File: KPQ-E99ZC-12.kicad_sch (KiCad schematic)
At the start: 25 parts, among them J1 USB Cable, J2 Chassis, J3 SWD, J4 Edge Connector, J5 Alternate Connector 1, J6 Alternate Connector 2, SW1 BOOT, U1 USBLC6-2SC6, U2 XC6206P332MR-G, U3 STM32C071KBT6

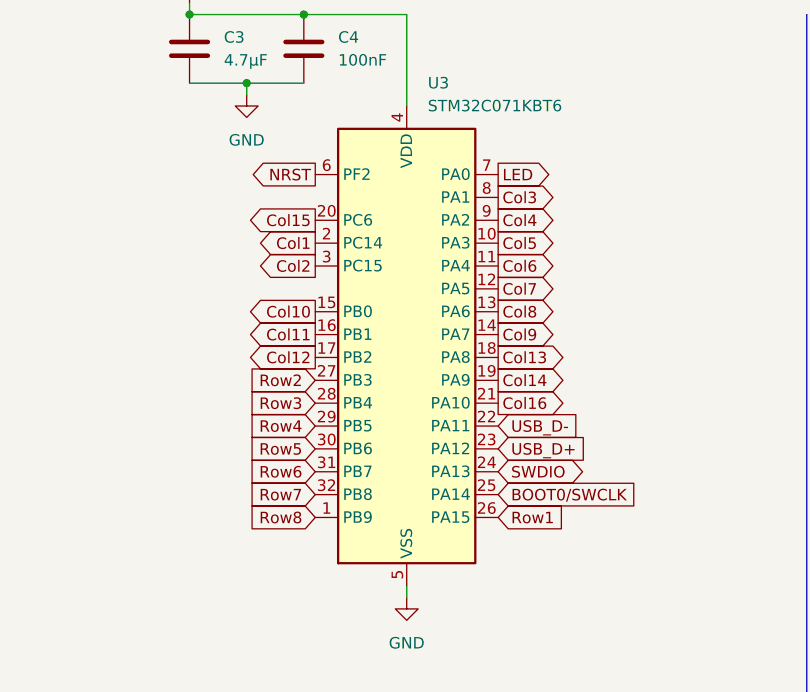
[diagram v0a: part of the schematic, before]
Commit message: Swap LED pin
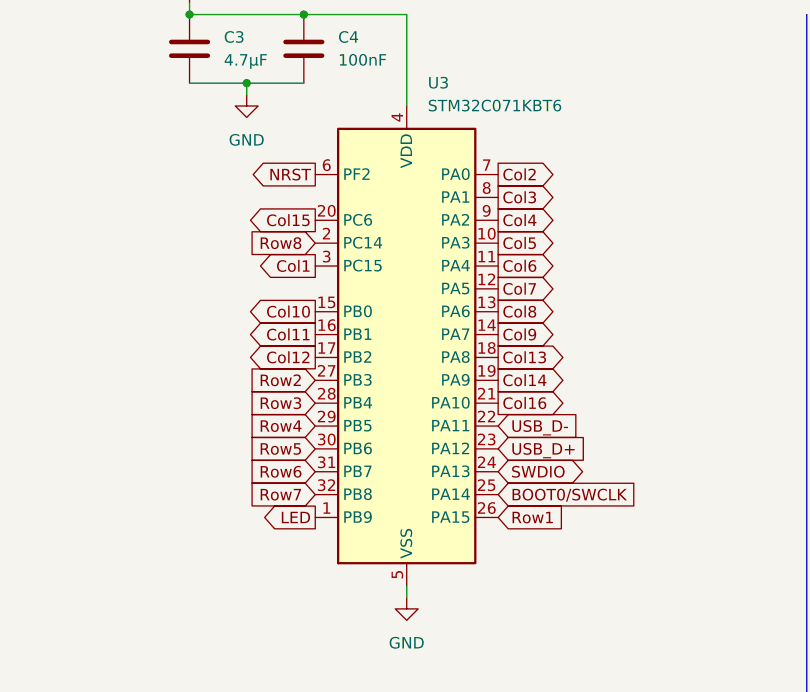
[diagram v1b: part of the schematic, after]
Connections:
- net Col1: now also U3.3 (PC15); no longer U3.2 (PC14)
- net Col2: now also U3.7 (PA0); no longer U3.3 (PC15)
- net LED: now also U3.1 (PB9); no longer U3.7 (PA0)
- net Row8: now also U3.2 (PC14); no longer U3.1 (PB9)
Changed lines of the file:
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@@
 	(global_label "Col2"
 		(shape output)
-		(at 171.45 83.82 180)
-		(fields_autoplaced yes)
-		(effects
-			(font
-				(size 1.27 1.27)
-			)
-			(justify right)
-		)
-		(property "Intersheetrefs" "${INTERSHEET_REFS}"
-			(at 165.2342 83.82 0)
-			(effects
-				(font
-					(size 1.27 1.27)
-				)
-				(justify right)
+		(at 191.77 73.66 0)
+		(fields_autoplaced yes)
+		(effects
+			(font
+				(size 1.27 1.27)
+			)
+			(justify left)
+		)
+		(property "Intersheetrefs" "${INTERSHEET_REFS}"
+			(at 197.9858 73.66 0)
+			(effects
+				(font
+					(size 1.27 1.27)
+				)
+				(justify left)
 				(hide yes)
 			)
@@
 	(global_label "Row8"
 		(shape input)
-		(at 171.45 111.76 180)
-		(fields_autoplaced yes)
-		(effects
-			(font
-				(size 1.27 1.27)
-			)
-			(justify right)
-		)
-		(property "Intersheetrefs" "${INTERSHEET_REFS}"
-			(at 164.2875 111.76 0)
+		(at 171.45 81.28 180)
+		(fields_autoplaced yes)
+		(effects
+			(font
+				(size 1.27 1.27)
+			)
+			(justify right)
+		)
+		(property "Intersheetrefs" "${INTERSHEET_REFS}"
+			(at 164.2875 81.28 0)
 			(effects
 				(font
@@
 	(global_label "LED"
 		(shape output)
-		(at 191.77 73.66 0)
-		(fields_autoplaced yes)
-		(effects
-			(font
-				(size 1.27 1.27)
-			)
-			(justify left)
-		)
-		(property "Intersheetrefs" "${INTERSHEET_REFS}"
-			(at 197.5254 73.66 0)
-			(effects
-				(font
-					(size 1.27 1.27)
-				)
-				(justify left)
+		(at 171.45 111.76 180)
+		(fields_autoplaced yes)
+		(effects
+			(font
+				(size 1.27 1.27)
+			)
+			(justify right)
+		)
+		(property "Intersheetrefs" "${INTERSHEET_REFS}"
+			(at 165.6946 111.76 0)
+			(effects
+				(font
+					(size 1.27 1.27)
+				)
+				(justify right)
 				(hide yes)
 			)
@@
 	(global_label "Col1"
 		(shape output)
-		(at 171.45 81.28 180)
-		(fields_autoplaced yes)
-		(effects
-			(font
-				(size 1.27 1.27)
-			)
-			(justify right)
-		)
-		(property "Intersheetrefs" "${INTERSHEET_REFS}"
-			(at 165.336 81.28 0)
-			(effects
-				(font
+		(at 171.45 83.82 180)
+		(fields_autoplaced yes)
+		(effects
+			(font
+				(size 1.27 1.27)
+			)
+			(justify right)
+		)
+		(property "Intersheetrefs" "${INTERSHEET_REFS}"
+			(at 165.336 83.82 0)
+			(effects
+				(font

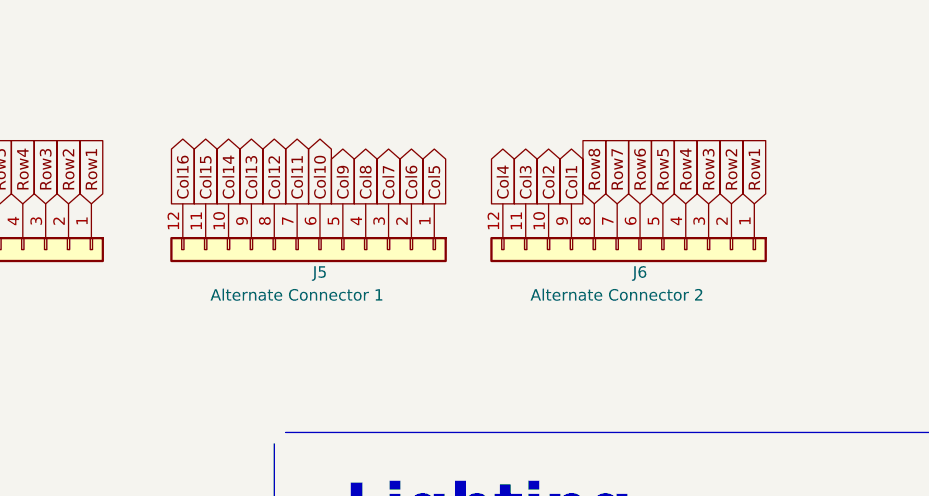
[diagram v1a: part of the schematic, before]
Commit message: Refine edges and positioning, especially around edge connectors
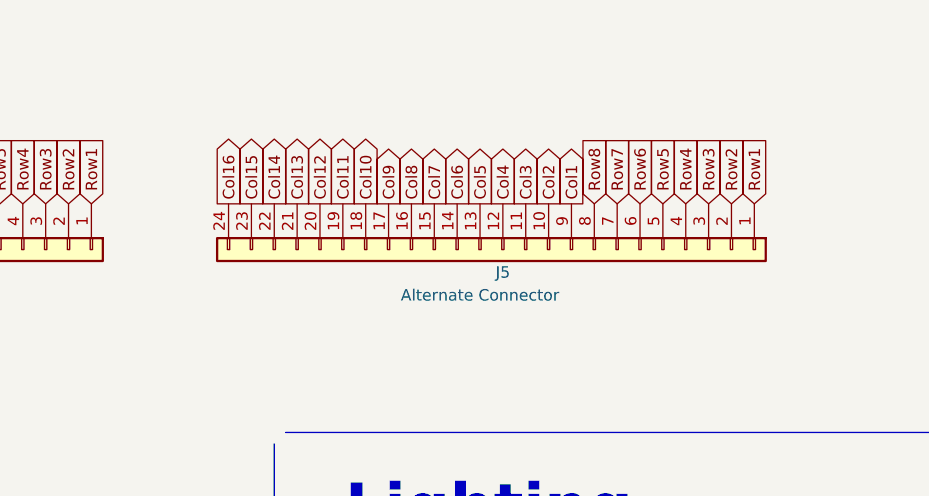
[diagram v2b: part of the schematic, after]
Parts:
- removed J5: Alternate Connector 1, Connector_PinHeader_2.54mm:PinHeader_1x12_P2.54mm_Vertical, symbol Connector_Generic:Conn_01x12
- J5: renamed from J6; value Alternate Connector 2 -> Alternate Connector; footprint Connector_PinHeader_2.54mm:PinHeader_1x12_P2.54mm_Vertical -> Connector_PinHeader_2.54mm:PinHeader_1x24_P2.54mm_Vertical; symbol Connector_Generic:Conn_01x12 -> Connector_Generic:Conn_01x24
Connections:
- net Col10: now also J5.18 (Pin_18)
- net Col11: now also J5.19 (Pin_19)
- net Col12: now also J5.20 (Pin_20)
- net Col13: now also J5.21 (Pin_21)
- net Col14: now also J5.22 (Pin_22)
- net Col15: now also J5.23 (Pin_23)
- net Col16: now also J5.24 (Pin_24)
- net Col5: now also J5.13 (Pin_13)
- net Col6: now also J5.14 (Pin_14)
- net Col7: now also J5.15 (Pin_15)
- net Col8: now also J5.16 (Pin_16)
- net Col9: now also J5.17 (Pin_17)
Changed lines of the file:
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@@
 	(global_label "Col16"
 		(shape output)
-		(at 215.9 29.21 90)
+		(at 220.98 29.21 90)
 		(fields_autoplaced yes)
 		(effects
@@
 		)
 		(property "Intersheetrefs" "${INTERSHEET_REFS}"
-			(at 215.9 22.1183 90)
+			(at 220.98 22.1183 90)
 			(effects
 				(font
@@
 	(global_label "Col8"
 		(shape output)
-		(at 236.22 29.21 90)
+		(at 241.3 29.21 90)
 		(fields_autoplaced yes)
 		(effects
@@
 		)
 		(property "Intersheetrefs" "${INTERSHEET_REFS}"
-			(at 236.22 22.8875 90)
+			(at 241.3 22.8875 90)
 			(effects
 				(font
@@
 	(global_label "Col11"
 		(shape output)
-		(at 228.6 29.21 90)
+		(at 233.68 29.21 90)
 		(fields_autoplaced yes)
 		(effects
@@
 		)
 		(property "Intersheetrefs" "${INTERSHEET_REFS}"
-			(at 228.6 22.2969 90)
+			(at 233.68 22.2969 90)
 			(effects
 				(font
@@
 	(global_label "Col13"
 		(shape output)
-		(at 223.52 29.21 90)
+		(at 228.6 29.21 90)
 		(fields_autoplaced yes)
 		(effects
@@
 		)
 		(property "Intersheetrefs" "${INTERSHEET_REFS}"
-			(at 223.52 22.1902 90)
+			(at 228.6 22.1902 90)
 			(effects
 				(font
@@
 	(global_label "Col5"
 		(shape output)
-		(at 243.84 29.21 90)
+		(at 248.92 29.21 90)
 		(fields_autoplaced yes)
 		(effects
@@
 		)
 		(property "Intersheetrefs" "${INTERSHEET_REFS}"
-			(at 243.84 22.9707 90)
+			(at 248.92 22.9707 90)
 			(effects
 				(font
@@
 	(global_label "Col7"
 		(shape output)
-		(at 238.76 29.21 90)
+		(at 243.84 29.21 90)
 		(fields_autoplaced yes)
 		(effects
@@
 		)
 		(property "Intersheetrefs" "${INTERSHEET_REFS}"
-			(at 238.76 23.0836 90)
+			(at 243.84 23.0836 90)
 			(effects
 				(font
@@
 	(global_label "Col10"
 		(shape output)
-		(at 231.14 29.21 90)
+		(at 236.22 29.21 90)
 		(fields_autoplaced yes)
 		(effects
@@
 		)
 		(property "Intersheetrefs" "${INTERSHEET_REFS}"
-			(at 231.14 22.0773 90)
+			(at 236.22 22.0773 90)
 			(effects
 				(font
@@
 	(global_label "Col15"
 		(shape output)
-		(at 218.44 29.21 90)
+		(at 223.52 29.21 90)
 		(fields_autoplaced yes)
 		(effects
@@
 		)
 		(property "Intersheetrefs" "${INTERSHEET_REFS}"
-			(at 218.44 22.1716 90)
+			(at 223.52 22.1716 90)
 			(effects
 				(font
@@
 	(global_label "Col6"
 		(shape output)
-		(at 241.3 29.21 90)
+		(at 246.38 29.21 90)
 		(fields_autoplaced yes)
 		(effects
@@
 		)
 		(property "Intersheetrefs" "${INTERSHEET_REFS}"
-			(at 241.3 22.9173 90)
+			(at 246.38 22.9173 90)
 			(effects
 				(font
@@
 	(global_label "Col9"
 		(shape output)
-		(at 233.68 29.21 90)
+		(at 238.76 29.21 90)
 		(fields_autoplaced yes)
 		(effects
@@
 		)
 		(property "Intersheetrefs" "${INTERSHEET_REFS}"
-			(at 233.68 22.9285 90)
+			(at 238.76 22.9285 90)
 			(effects
 				(font
@@
 	(global_label "Col12"
 		(shape output)
-		(at 226.06 29.21 90)
+		(at 231.14 29.21 90)
 		(fields_autoplaced yes)
 		(effects
@@
 		)
 		(property "Intersheetrefs" "${INTERSHEET_REFS}"
-			(at 226.06 22.1952 90)
+			(at 231.14 22.1952 90)
 			(effects
 				(font
@@
 	(global_label "Col14"
 		(shape output)
-		(at 220.98 29.21 90)
+		(at 226.06 29.21 90)
 		(fields_autoplaced yes)
 		(effects
@@
 		)
 		(property "Intersheetrefs" "${INTERSHEET_REFS}"
-			(at 220.98 22.1183 90)
+			(at 226.06 22.1183 90)
 			(effects
 				(font
@@
 	)
 	(symbol
-		(lib_id "Connector_Generic:Conn_01x12")
-		(at 266.7 34.29 270)
+		(lib_id "Connector_Generic:Conn_01x24")
+		(at 251.46 34.29 270)
 		(unit 1)
 		(exclude_from_sim no)
@@
 		(on_board yes)
 		(dnp no)
-		(property "Reference" "J6"
-			(at 266.7 36.83 90)
+		(property "Reference" "J5"
+			(at 251.46 36.83 90)
 			(effects
 				(font
@@
 			)
 		)
-		(property "Value" "Alternate Connector 2"
-			(at 264.16 39.37 90)
+		(property "Value" "Alternate Connector"
+			(at 248.92 39.37 90)
 			(effects
 				(font
@@
 			)
 		)
-		(property "Footprint" "Connector_PinHeader_2.54mm:PinHeader_1x12_P2.54mm_Vertical"
-			(at 266.7 34.29 0)
+		(property "Footprint" "Connector_PinHeader_2.54mm:PinHeader_1x24_P2.54mm_Vertical"
+			(at 251.46 34.29 0)
 			(effects
 				(font
@@
 		)
 		(property "Datasheet" "~"
-			(at 266.7 34.29 0)
+			(at 251.46 34.29 0)
 			(effects
 				(font
@@
 			)
 		)
-		(property "Description" "Generic connector, single row, 01x12, script generated (kicad-library-utils/schlib/autogen/connector/)"
-			(at 266.7 34.29 0)
+		(property "Description" "Generic connector, single row, 01x24, script generated (kicad-library-utils/schlib/autogen/connector/)"
+			(at 251.46 34.29 0)
 			(effects
 				(font
@@
 		(pin "10"
 		)
+		(pin "13"
+		)
+		(pin "14"
+		)
+		(pin "15"
+		)
+		(pin "16"
+		)
+		(pin "17"
+		)
+		(pin "18"
+		)
+		(pin "19"
+		)
+		(pin "20"
+		)
+		(pin "21"
+		)
+		(pin "22"
+		)
+		(pin "23"
+		)
+		(pin "24"
+		)
 		(instances
 			(project "KPQ-E99ZC-12"
 				(path "/2ca696f5-3b9d-4437-b6f7-98ba53a6592e"
-					(reference "J6")
+					(reference "J5")
 					(unit 1)
 				)
@@
 					(unit 1)
 				)
-			)
-		)
-	)
-	(symbol
-		(lib_id "Connector_Generic:Conn_01x12")
-		(at 231.14 34.29 270)
-		(unit 1)
-		(exclude_from_sim no)
-		(in_bom yes)
-		(on_board yes)
-		(dnp no)
-		(property "Reference" "J5"
-			(at 231.14 36.83 90)
-			(effects
-				(font
-					(size 1.27 1.27)
-				)
-			)
-		)
-		(property "Value" "Alternate Connector 1"
-			(at 228.6 39.37 90)
-			(effects
-				(font
-					(size 1.27 1.27)
-				)
-			)
-		)
-		(property "Footprint" "Connector_PinHeader_2.54mm:PinHeader_1x12_P2.54mm_Vertical"
-			(at 231.14 34.29 0)
-			(effects
-				(font
-					(size 1.27 1.27)
-				)
-				(hide yes)
-			)
-		)
-		(property "Datasheet" "~"
-			(at 231.14 34.29 0)
-			(effects
-				(font
-					(size 1.27 1.27)
-				)
-				(hide yes)
-			)
-		)
-		(property "Description" "Generic connector, single row, 01x12, script generated (kicad-library-utils/schlib/autogen/connector/)"
-			(at 231.14 34.29 0)
-			(effects
-				(font
-					(size 1.27 1.27)
-				)
-				(hide yes)
-			)
-		)
-		(pin "4"
-		)
-		(pin "1"
-		)
-		(pin "7"
-		)
-		(pin "12"
-		)
-		(pin "11"
-		)
-		(pin "2"
-		)
-		(pin "5"
-		)
-		(pin "9"
-		)
-		(pin "3"
-		)
-		(pin "6"
-		)
-		(pin "8"
-		)
-		(pin "10"
-		)
-		(instances
-			(project "KPQ-E99ZC-12"
-				(path "/2ca696f5-3b9d-4437-b6f7-98ba53a6592e"
-					(reference "J5")
-					(unit 1)
-				)
